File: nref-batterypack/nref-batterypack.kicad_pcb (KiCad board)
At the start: 2 copper layers, 75 x 17 mm, 53 parts, among them J1 C3-, J2 DBG, J3 PACK_CONN, J4 C4+, J5 C2+, J6 C1-, J7 C1-, J8 BACK_CONN, SW1 Reset, U1 BQ76905, U2 TPS259482, U3 MSPM0L130xRGE

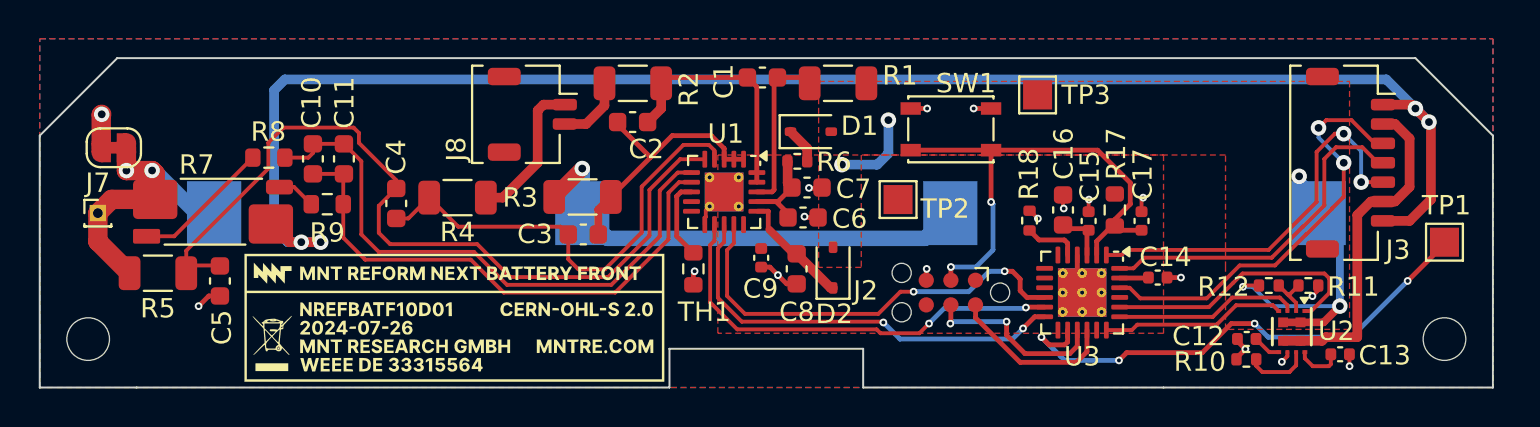
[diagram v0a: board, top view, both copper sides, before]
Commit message: v2 of the bms now based on the final outline
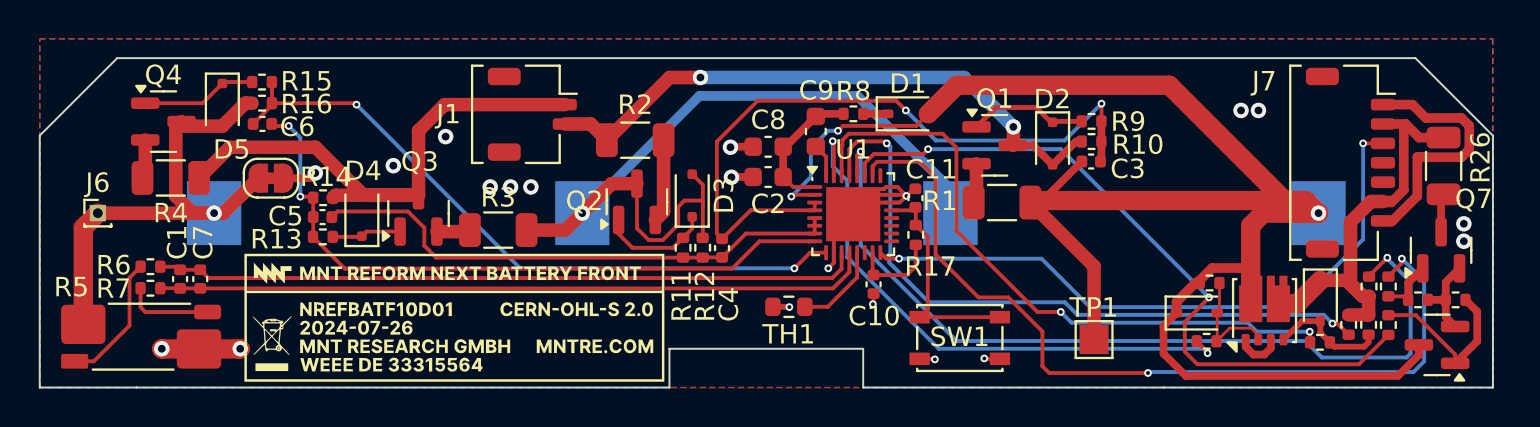
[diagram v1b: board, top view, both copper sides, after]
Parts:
- removed C12: 2.2nF, Capacitor_SMD:C_0402_1005Metric
- removed C13: DNP, Capacitor_SMD:C_0402_1005Metric
- removed C14: 0.47uF, Capacitor_SMD:C_0402_1005Metric
- removed C15, C17: 100nF, Capacitor_SMD:C_0402_1005Metric
- removed C16: 10uF, Capacitor_SMD:C_0603_1608Metric
- removed the J2 at (147.0, 103.1)
- removed REF** (x2): MountingHole_2.2mm_M2, MountingHole:MountingHole_2.2mm_M2
- removed TP2: 3V3, TestPoint:TestPoint_Pad_1.5x1.5mm
- removed TP3: Pack Voltage, TestPoint:TestPoint_Pad_1.5x1.5mm
- removed U2: TPS259482, Automated:PowerWCSP12_YWP_TEX
- removed U3: MSPM0L130xRGE, Package_DFN_QFN:VQFN-24-1EP_4x4mm_P0.5mm_EP2.5x2.5mm_ThermalVias
- added D3: 30V, Diode_SMD:D_SOD-323F, F.Cu at (133.7, 98.1)
- added D4: 30V, Diode_SMD:D_SOD-323F, F.Cu at (116.6, 99.1)
- added D5: 30V, Diode_SMD:D_SOD-323F, F.Cu at (109.4, 93.4)
- added D6: 16V, Diode_SMD:D_SOD-323, F.Cu at (159.7, 104.2)
- added D7: 16V, Diode_SMD:D_SOD-323, F.Cu at (166.1, 103.5)
- added Q1: BC817, Package_TO_SOT_SMD:SOT-23, F.Cu at (149.3, 95.5)
- added Q2: BC817, Package_TO_SOT_SMD:SOT-23, F.Cu at (130.8, 98.4)
- added Q3: BC817, Package_TO_SOT_SMD:SOT-23, F.Cu at (119.5, 99.0)
- added Q4: BC817, Package_TO_SOT_SMD:SOT-23, F.Cu at (106.4, 94.3)
- added Q5: AO3401A, Package_TO_SOT_SMD:SOT-23, F.Cu at (172.1, 105.8)
- added Q6: DMT2005UDV, Automated:Diodes_PowerDI3333-8_UXC_3.3x3.3mm_P0.65mm, F.Cu at (163.2, 104.0)
- added Q7: AO3401A, Package_TO_SOT_SMD:SOT-23, F.Cu at (172.3, 100.9)
- added R13: 240R, Resistor_SMD:R_0402_1005Metric, F.Cu at (114.6, 100.2)
- added R14: 100R, Resistor_SMD:R_0402_1005Metric, F.Cu at (114.6, 98.2)
- added R15: 240R, Resistor_SMD:R_0402_1005Metric, F.Cu at (111.5, 92.2)
- added R16: 100R, Resistor_SMD:R_0402_1005Metric, F.Cu at (111.5, 93.3)
- added R19: 5.1k, Resistor_SMD:R_0402_1005Metric, F.Cu at (169.6, 104.8)
- added R20: 5.1k, Resistor_SMD:R_0402_1005Metric, F.Cu at (160.2, 105.6)
- added R21: 10M, Resistor_SMD:R_0402_1005Metric, F.Cu at (173.1, 103.5)
- added R22: 10M, Resistor_SMD:R_0402_1005Metric, F.Cu at (171.1, 103.5)
- added R23: 5.1k, Resistor_SMD:R_0402_1005Metric, F.Cu at (166.1, 105.7)
- added R24: 5.1k, Resistor_SMD:R_0402_1005Metric, F.Cu at (169.6, 102.8)
- added R25: 10M, Resistor_SMD:R_0402_1005Metric, F.Cu at (168.6, 104.8)
- added R26: 1k, Resistor_SMD:R_1206_3216Metric, F.Cu at (172.5, 96.6)
- added R27: 10k, Resistor_SMD:R_0402_1005Metric, F.Cu at (168.6, 102.8)
- added R28: 10k, Resistor_SMD:R_0402_1005Metric, F.Cu at (167.6, 104.8)
- C1: value 220nF -> 100nF; footprint Capacitor_SMD:C_0603_1608Metric -> Capacitor_SMD:C_0402_1005Metric
- C10: value 100pF -> 2.2uF; footprint Capacitor_SMD:C_0603_1608Metric -> Capacitor_SMD:C_0402_1005Metric
- C11, C3, C4, C5: footprint Capacitor_SMD:C_0603_1608Metric -> Capacitor_SMD:C_0402_1005Metric
- C2: value 220nF -> 100pF/25V
- C6: value 100pF/25V -> 220nF; footprint Capacitor_SMD:C_0603_1608Metric -> Capacitor_SMD:C_0402_1005Metric
- C7: value 1uF/25V -> 100pF; footprint Capacitor_SMD:C_0603_1608Metric -> Capacitor_SMD:C_0402_1005Metric
- C9: value 1uF -> 470nF/25V; footprint Capacitor_SMD:C_0402_1005Metric -> Capacitor_SMD:C_0603_1608Metric
- D2: value 40V -> 30V; footprint Diode_SMD:D_SOD-323 -> Diode_SMD:D_SOD-323F
- R1, R2, R3, R4: value 10R -> 49.9R
- R10: value 866R -> 100R
- R11: value 14.7k -> 240R
- R12: value 470k -> 100R
- R17, R8: footprint Resistor_SMD:R_0603_1608Metric -> Resistor_SMD:R_0402_1005Metric
- R18: value 100k/0.1%/25ppm -> 10M
- R5: value 10R -> 1u; footprint Resistor_SMD:R_1206_3216Metric -> Resistor_SMD:R_Shunt_Vishay_WSK2512_6332Metric_T1.19mm
- R7: value 1u -> 100R; footprint Resistor_SMD:R_Shunt_Vishay_WSK2512_6332Metric_T1.19mm -> Resistor_SMD:R_0402_1005Metric
- R9: value 100R -> 240R; footprint Resistor_SMD:R_0603_1608Metric -> Resistor_SMD:R_0402_1005Metric
- TP1: value BSL Invoke -> Pack Voltage
- U1: value BQ76905 -> BQ76922; footprint Package_DFN_QFN:QFN-20-1EP_3.5x3.5mm_P0.5mm_EP2x2mm_ThermalVias -> Package_DFN_QFN:Texas_RSN_WQFN-32-1EP_4x4mm_P0.4mm_EP2.8x2.8mm
- moved R9 39.7 mm to (154.3, 94.3), turned to 180 degrees
- moved R6 33.8 mm to (105.7, 101.8)
- moved R11 32.3 mm to (133.2, 100.8), turned to 90 degrees
- moved C1 31.8 mm to (107.2, 102.4), turned to -90 degrees
- moved C7 31.7 mm to (108.3, 102.4), turned to -90 degrees
- moved R8 30.3 mm to (142.0, 93.9)
- moved C10 29.7 mm to (143.0, 102.7), turned to 90 degrees
- moved C11 29.6 mm to (145.2, 98.2)
- moved R12 29.3 mm to (134.2, 100.8), turned to 90 degrees
- moved C6 28.3 mm to (111.5, 94.4), turned to 180 degrees
- moved C3 26.5 mm to (154.3, 96.3), turned to 0 degrees
- moved TP1 18.8 mm to (154.4, 105.5)
- moved C4 17.0 mm to (135.2, 100.8), turned to -90 degrees
- moved R4 14.8 mm to (106.8, 97.2), turned to 180 degrees
- moved R10 13.8 mm to (154.3, 95.3), turned to 180 degrees
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- renumbered J8 to J1, J4 to J2, J1 to J3, J5 to J4, J6 to J5, J7 to J6, J3 to J7
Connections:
- net /V_{OUT} renamed /PACK+
- C1 pad 1: Net-(U1-VC5) -> /SRP
- C1 pad 2: Net-(U1-VC4A) -> /SRN
- C10 pad 1: Net-(U1-SRP) -> GND
- C10 pad 2: Net-(U1-SRN) -> +1V8
- C11 pad 1: Net-(U1-SRP) -> GND
- C11 pad 2: Net-(U1-SRN) -> /~{RST}
- C2 pad 1: Net-(U1-VC4A) -> Net-(U1-BAT)
- C2 pad 2: Net-(U1-VC2) -> GND
- C3 pad 1: Net-(U1-VC2) -> /BAT+
- C3 pad 2: Net-(U1-VC1) -> /VC4
- C4 pad 1: Net-(U1-VC1) -> /VC4
- C4 pad 2: Net-(U1-VC0) -> /VC2
- C5 pad 1: Net-(U1-VC0) -> /VC2
- C5 pad 2: GND -> /VC1
- C6 pad 1: Net-(U1-BAT) -> /VC1
- C6 pad 2: GND -> /VC0
- C7 pad 1: Net-(U1-BAT) -> /SRP
- C7 pad 2: GND -> /SRN
- C8 pad 1: /REGSRC -> Net-(U1-BAT)
- C9 pad 1: +3V3 -> Net-(U1-CP1)
- C9 pad 2: GND -> Net-(U1-BAT)
- D1 pad 2: IN -> /BAT+
- D2 pad 1: /REGSRC -> Net-(D2-K)
- D2 pad 2: IN -> /C3+
- J2 pad 1: IN -> /BAT+
- J3 pad 1: /C2+ -> Net-(D3-A)
- J4 pad 1: /C2+ -> Net-(D3-A)
- J7 pad 3: /IRQ -> /ALERT
- R1 pad 1: Net-(U1-VC5) -> /BAT+
- R1 pad 2: IN -> Net-(Q1-C)
- R10 pad 1: GND -> /VC4
- R10 pad 2: Net-(U2-ILM) -> /C3+
- R11 pad 1: GND -> /VC2
- R11 pad 2: Net-(U2-OVLO) -> Net-(D3-K)
- R12 pad 1: Net-(U2-OVLO) -> /VC2
- R12 pad 2: IN -> Net-(D3-A)
- R17 pad 2: +3V3 -> +1V8
- R18 pad 1: GND -> Net-(D6-A)
- R18 pad 2: Net-(U3-PA2) -> /BAT+
- R2 pad 1: Net-(U1-VC4A) -> /C3+
- R2 pad 2: /C3+ -> Net-(Q2-C)
- R3 pad 1: Net-(U1-VC2) -> Net-(D3-A)
- R3 pad 2: /C2+ -> Net-(Q3-C)
- R4 pad 1: Net-(U1-VC1) -> /C1+
- R4 pad 2: /C1+ -> Net-(Q4-C)
- R5 pad 1: Net-(U1-VC0) -> /BAT-
- R5 pad 2: /BAT- -> Net-(R5-Pad2)
- R6 pad 1: Net-(U1-BAT) -> Net-(R5-Pad2)
- R6 pad 2: Net-(D1-K) -> /SRP
- R7 pad 1: /BAT- -> Net-(R5-Pad3)
- R7 pad 2: Net-(R7-Pad2) -> /SRN
- R8 pad 1: Net-(R7-Pad2) -> Net-(U1-BAT)
- R8 pad 2: Net-(U1-SRP) -> Net-(D1-K)
- R9 pad 1: Net-(R7-Pad3) -> /VC4
- R9 pad 2: Net-(U1-SRN) -> Net-(D2-K)
- TH1 pad 1: Net-(U1-TS) -> Net-(U1-TS1)
- TP1 pad 1: /BSL_INVOKE -> /BAT+
- U1 pad 1: Net-(U1-VC2) -> Net-(U1-BAT)
- U1 pad 10: unconnected-(U1-CHG-Pad10) -> GND
- U1 pad 11: GND -> /SRP
- U1 pad 12: /SCL_{DEV} -> /SRN
- U1 pad 13: /SDA_{DEV} -> Net-(U1-TS1)
- U1 pad 14: /ALERT -> unconnected-(U1-TS2-Pad14)
- U1 pad 15: +3V3 -> +1V8
- U1 pad 16: /REGSRC -> /ALERT
- U1 pad 17: Net-(U1-BAT) -> /SCL_{DEV}
- U1 pad 18: Net-(U1-VC5) -> /SDA_{DEV}
- U1 pad 19: Net-(U1-VC4A) -> unconnected-(U1-CFETOFF-Pad19)
- U1 pad 2: Net-(U1-VC2) -> /BAT+
- U1 pad 20: Net-(U1-VC4A) -> unconnected-(U1-DFETOFF-Pad20)
- U1 pad 21: GND -> /~{RST}
- U1 pad 3: Net-(U1-VC2) -> /VC4
- U1 pad 4: Net-(U1-VC1) -> /VC4
- U1 pad 5: Net-(U1-VC0) -> /VC2
- U1 pad 6: Net-(U1-SRP) -> /VC2
- U1 pad 7: Net-(U1-SRN) -> /VC2
- U1 pad 8: Net-(U1-TS) -> /VC1
- U1 pad 9: unconnected-(U1-DSG-Pad9) -> /VC0
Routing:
- net /BAT+: track 0.00 -> 93.2 mm, vias 0 -> 3
- net /PACK-: track 83.3 -> 17.4 mm, vias 4 -> 11
- net /PDSG: track 0.00 -> 44.2 mm, vias 0 -> 2
- net /LD: track 0.00 -> 43.8 mm, vias 0 -> 2
- net Net-(U1-VC0): track 43.5 -> 0.00 mm
- net Net-(D3-A): track 0.00 -> 42.3 mm, vias 0 -> 1
- net /SRN: track 0.00 -> 36.9 mm
- net /PCHG: track 0.00 -> 36.6 mm, vias 0 -> 2
- net /SRP: track 0.00 -> 36.4 mm
- net /VC4: track 0.00 -> 36.3 mm, vias 0 -> 2
- net /VC0: track 0.00 -> 35.0 mm, vias 0 -> 2
- net /PACK: track 0.00 -> 35.0 mm, vias 0 -> 2
- net /VC1: track 0.00 -> 34.7 mm, vias 0 -> 2
- net /DSG: track 0.00 -> 33.4 mm, vias 0 -> 2
- net Net-(U1-SRP): track 30.6 -> 0.00 mm
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- added copper zone on B.Cu, net /PACK-
- added copper zone on In1.Cu, net GND
- added copper zone on In2.Cu, net GND
- removed copper zone on F.Cu, net +3V3
- removed copper zone on B.Cu, net GND
- removed copper zone on F.Cu, net IN
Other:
- copper layers 2 -> 4

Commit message: batterypack: pick parts
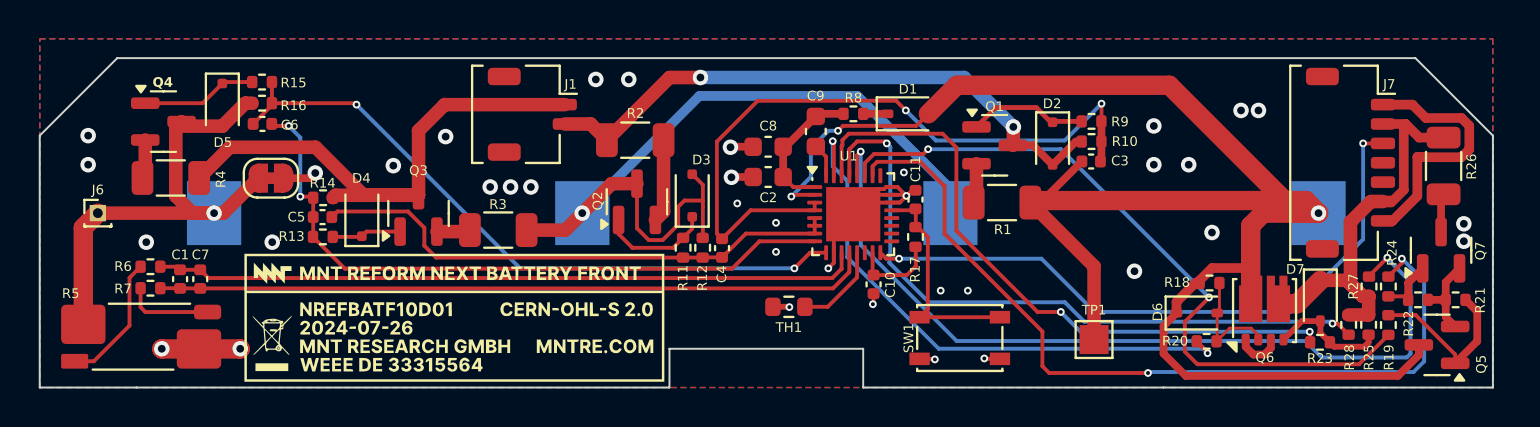
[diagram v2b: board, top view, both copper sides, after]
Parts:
- moved R17 0.11 mm to (145.2, 100.2)
- moved C11 0.08 mm to (145.2, 98.3)
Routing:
- net /PDSG: track 44.2 -> 43.3 mm
- net GND: vias 9 -> 15
- net /PACK-: vias 11 -> 22

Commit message: fix load switch nmos and gate prot diode polarity
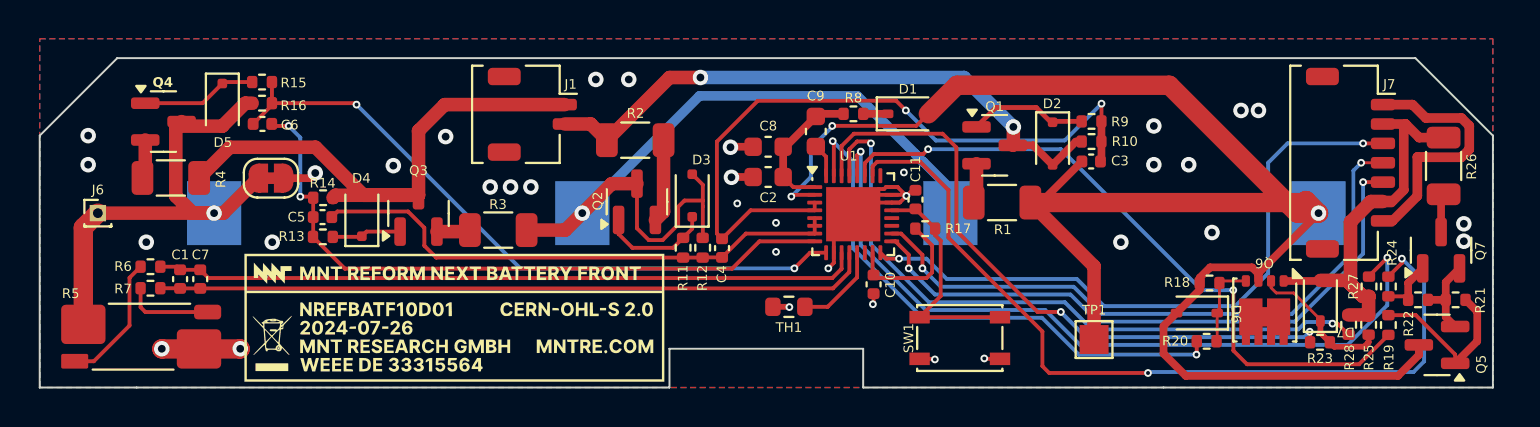
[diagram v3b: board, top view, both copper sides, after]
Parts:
- moved R17 0.66 mm to (145.7, 99.8), turned to 180 degrees
- turned Q6 to -90 degrees
- turned D6 to 180 degrees
- turned D7 to 90 degrees
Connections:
- D6 pad 1: /BAT+ -> Net-(D6-K)
- D6 pad 2: Net-(D6-A) -> /BAT+
- D7 pad 1: /PACK+ -> Net-(D7-K)
- D7 pad 2: Net-(D7-A) -> /PACK+
- J7 pad 4: /SDA_{HOST} -> /SDA
- J7 pad 5: /SCL_{HOST} -> /SCL
- Q6 pad 1: Net-(Q6A-S) -> /PACK+
- Q6 pad 2: Net-(D6-A) -> Net-(D7-K)
- Q6 pad 3: Net-(Q6A-S) -> /BAT+
- Q6 pad 4: Net-(D7-A) -> Net-(D6-K)
- Q6 pad 5: /PACK+ -> Net-(Q6A-D)
- Q6 pad 6: /BAT+ -> Net-(Q6A-D)
- R18 pad 1: Net-(D6-A) -> Net-(D6-K)
- R20 pad 2: Net-(D6-A) -> Net-(D6-K)
- R23 pad 2: Net-(D7-A) -> Net-(D7-K)
- R25 pad 1: Net-(D7-A) -> Net-(D7-K)
- U1 pad 17: /SCL_{DEV} -> /SCL
- U1 pad 18: /SDA_{DEV} -> /SDA
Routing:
- net /SDA: track 0.00 -> 33.2 mm, vias 0 -> 2
- net /SCL: track 0.00 -> 32.6 mm, vias 0 -> 2
- net Net-(D7-K): track 0.00 -> 7.53 mm
- net Net-(D7-A): track 6.18 -> 0.00 mm
- net Net-(D6-A): track 5.89 -> 0.00 mm
- net Net-(D6-K): track 0.00 -> 4.48 mm
- net /LD: track 43.8 -> 40.1 mm
- net /BAT+: track 93.2 -> 89.6 mm
- net Net-(Q6A-S): track 2.40 -> 0.00 mm
- net +1V8: track 4.64 -> 7.00 mm
- net /PCHG: track 36.6 -> 35.0 mm
- net Net-(Q6A-D): track 0.00 -> 1.43 mm
- net /CHG: track 29.6 -> 28.5 mm
- net /PACK+: track 21.9 -> 21.2 mm
- net GND: vias 15 -> 13

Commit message: added reverse polarity indicator LEDs
+ silk on the back to indicate cell polarity
+ updated resistor values for balancing
* better b2b chg, dsg fets
+ more testpoints
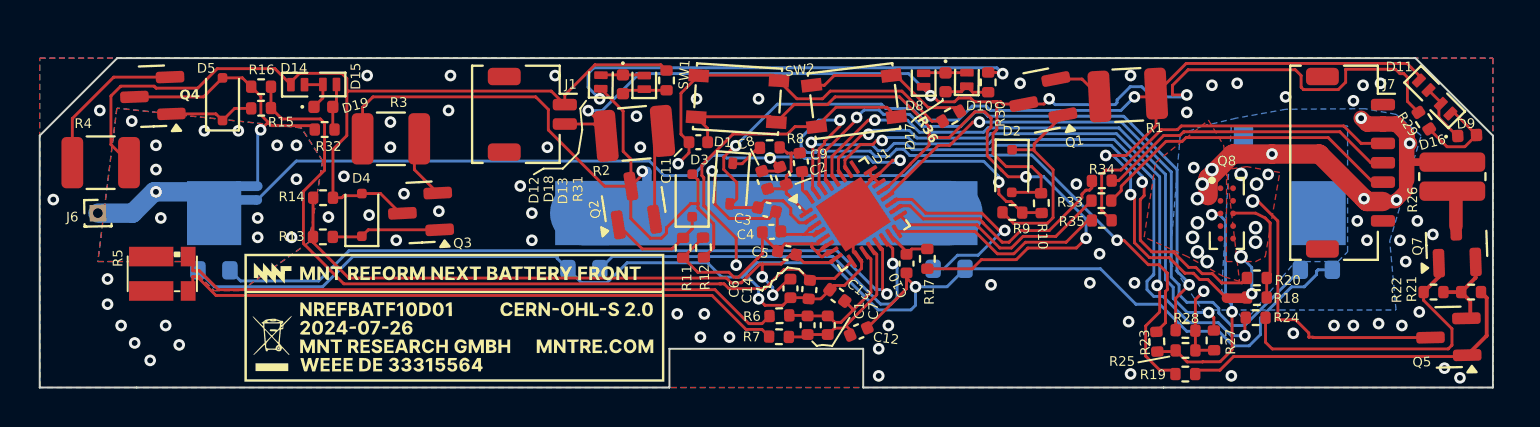
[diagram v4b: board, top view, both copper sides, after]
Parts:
- removed D6, D7: 16V, Diode_SMD:D_SOD-323
- removed Q6: DMT2005UDV, Automated:Diodes_PowerDI3333-8_UXC_3.3x3.3mm_P0.65mm
- added C12: 100nF, Capacitor_SMD:C_0402_1005Metric, F.Cu at (142.3, 105.1)
- added C13: 100nF, Capacitor_SMD:C_0402_1005Metric, F.Cu at (141.2, 103.2)
- added C14: 100nF, Capacitor_SMD:C_0402_1005Metric, F.Cu at (139.7, 102.9)
- added D10: BAS70LP, Diode_SMD:D_SOD-882, F.Cu at (147.8, 92.1)
- added D11: BAS70LP, Diode_SMD:D_SOD-882, F.Cu at (171.4, 92.4)
- added D12: BAS70LP, Diode_SMD:D_SOD-882, F.Cu at (129.0, 92.2)
- added D13: BAS70LP, Diode_SMD:D_SOD-882, F.Cu at (131.2, 92.2)
- added D14: BAS70LP, Diode_SMD:D_SOD-882, F.Cu at (113.3, 92.4)
- added D15: BAS70LP, Diode_SMD:D_SOD-882, F.Cu at (115.0, 92.4)
- added D16: BAS70LP, Diode_SMD:D_SOD-882, F.Cu at (172.6, 93.6)
- added D17: Red, LED_SMD:LED_0402_1005Metric, F.Cu at (146.8, 92.2)
- added D18: Red, LED_SMD:LED_0402_1005Metric, F.Cu at (130.1, 92.3)
- added D19: Red, LED_SMD:LED_0402_1005Metric, F.Cu at (114.6, 93.5)
- added D8: BAS70LP, Diode_SMD:D_SOD-882, F.Cu at (145.6, 92.1)
- added D9: Red, LED_SMD:LED_0402_1005Metric, F.Cu at (173.7, 95.0)
- added NT3: P- to GND, NetTie:NetTie-2_SMD_Pad0.5mm, B.Cu at (131.3, 97.3)
- added NT4.0: P- to GND, NetTie:NetTie-2_SMD_Pad0.5mm, F.Cu at (161.8, 103.4)
- added NT5: P- to GND, NetTie:NetTie-2_SMD_Pad0.5mm, B.Cu at (110.8, 97.6)
- added Q8: Q_Dual_NMOS_Picostar_CSD87501L, Automated:TI_PICOSTAR_LGA-10_3.37x1.47mm_P0.65mm, F.Cu at (161.3, 99.0)
- added R29: 100, Resistor_SMD:R_0402_1005Metric, F.Cu at (171.4, 94.2)
- added R30: 100, Resistor_SMD:R_0402_1005Metric, F.Cu at (148.9, 92.2)
- added R31: 100, Resistor_SMD:R_0402_1005Metric, F.Cu at (132.3, 92.2)
- added R32: 100, Resistor_SMD:R_0402_1005Metric, F.Cu at (114.7, 94.7)
- added R33: 100, Resistor_SMD:R_0402_1005Metric, F.Cu at (154.8, 98.4)
- added R34: 100, Resistor_SMD:R_0402_1005Metric, F.Cu at (154.8, 97.3)
- added R35: 100, Resistor_SMD:R_0402_1005Metric, F.Cu at (154.8, 99.4)
- added R36: 10k, Resistor_SMD:R_0402_1005Metric, F.Cu at (147.0, 94.0)
- added SW2: Wake, Button_Switch_SMD:SW_SPST_PTS810, F.Cu at (142.0, 93.2)
- added TH2: Thermistor, Resistor_SMD:R_0603_1608Metric, B.Cu at (128.1, 101.9)
- added TH3: Thermistor, Resistor_SMD:R_0603_1608Metric, B.Cu at (146.9, 101.9)
- added TH4: Thermistor, Resistor_SMD:R_0603_1608Metric, B.Cu at (165.9, 101.9)
- C2: value 100pF/25V -> 100pF; footprint Capacitor_SMD:C_0603_1608Metric -> Capacitor_SMD:C_0402_1005Metric
- C3, C4, C5, C6: value 220nF -> 100nF
- C8: value 1uF/25V -> 2.2uF/25V; footprint Capacitor_SMD:C_0603_1608Metric -> Capacitor_SMD:C_0402_1005Metric
- C9: footprint Capacitor_SMD:C_0603_1608Metric -> Capacitor_SMD:C_0402_1005Metric
- D2, D3, D4, D5: value 30V -> BAS70LP
- J2, J3, J4, J5: footprint footprints:S713145R -> Automated:S713145R
- NT1: value P- to GND -> P- to VSS; footprint Jumper:SolderJumper-2_P1.3mm_Bridged_RoundedPad1.0x1.5mm -> NetTie:NetTie-2_SMD_Pad0.5mm; moved to B.Cu
- R1, R2, R3, R4: value 49.9R -> 39; footprint Resistor_SMD:R_1206_3216Metric -> Resistor_SMD:R_1210_3225Metric
- R10, R12, R14, R16, R17, R6, R7, R8: value 100R -> 100
- R11, R13, R15, R9: value 240R -> 240
- R19, R20, R23, R24: value 5.1k -> 1k
- R26: value 1k -> 270; footprint Resistor_SMD:R_1206_3216Metric -> Resistor_SMD:R_0612_1632Metric
- R5: value 1u -> 15mΩ 1%; footprint Resistor_SMD:R_Shunt_Vishay_WSK2512_6332Metric_T1.19mm -> Automated:R_Shunt_Kelvin_Littlefuse_L4CA
- TH1: moved to B.Cu
- TP1: footprint TestPoint:TestPoint_Pad_1.5x1.5mm -> TestPoint:TestPoint_Pad_1.0x1.0mm; moved to B.Cu
- moved R6 32.6 mm to (138.2, 104.3), turned to 2 degrees
- moved R7 32.5 mm to (138.2, 105.4), turned to -1 degrees
- moved C1 32.5 mm to (139.6, 104.8)
- moved C7 32.5 mm to (140.7, 104.8)
- moved TH1 29.7 mm to (109.0, 101.9)
- moved C6 28.5 mm to (138.7, 102.9), turned to -90 degrees
- moved C5 24.0 mm to (138.6, 101.1), turned to -11.35 degrees
- moved C3 16.9 mm to (137.5, 98.8), turned to -12.8 degrees
- moved SW1 16.8 mm to (136.0, 93.1), turned to -3.6 degrees
- moved TP1 13.0 mm to (162.1, 95.0), turned to 89.3 degrees
- moved C11 11.6 mm to (134.0, 95.3), turned to 0 degrees
- moved R19 10.8 mm to (159.1, 107.3), turned to 0 degrees
- moved D1 9.80 mm to (135.7, 97.5), turned to -94.23 degrees
- moved R25 9.54 mm to (159.1, 106.1), turned to 0 degrees
- moved R1 8.54 mm to (156.2, 92.9), turned to -177 degrees
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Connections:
- net /PACK renamed /bqPACK
- net /SRN renamed /SR_N
- net /SRP renamed /SR_P
- net Net-(R5-Pad2) renamed /CSENSE_P
- net Net-(R5-Pad3) renamed /CSENSE_N
- net Net-(U1-BAT) renamed /bqBAT
- net Net-(U1-TS1) renamed /TS1
- C10 pad 1: GND -> VSS
- C2 pad 2: GND -> VSS
- C3 pad 1: /BAT+ -> /VC5
- C6 pad 2: /VC0 -> VSS
- C8 pad 2: GND -> VSS
- D1 pad 2: /BAT+ -> /VC5
- D3 pad 2: Net-(D3-A) -> Net-(D12-K)
- D5 pad 2: /BAT- -> Net-(D5-A)
- J2 pad 1: /BAT+ -> /BATplus
- J3 pad 1: Net-(D3-A) -> /Cell23
- J4 pad 1: Net-(D3-A) -> /Cell23
- J7 pad 1: /PACK- -> GND
- J7 pad 7: /PACK- -> GND
- NT1 pad 1: GND -> VSS
- Q2 pad 3: Net-(D3-A) -> Net-(D12-K)
- Q4 pad 3: /BAT- -> Net-(D5-A)
- Q5 pad 3: /BAT+ -> /BATplus
- R1 pad 1: /BAT+ -> /VC5
- R12 pad 2: Net-(D3-A) -> Net-(D12-K)
- R16 pad 2: /BAT- -> Net-(D5-A)
- R18 pad 2: /BAT+ -> /BATplus
- R3 pad 1: Net-(D3-A) -> Net-(D12-K)
- R5 pad 4: /PACK- -> GND
- TH1 pad 2: GND -> VSS
- TP1 pad 1: /BAT+ -> /BATplus
- U1 pad 10: GND -> VSS
- U1 pad 14: unconnected-(U1-TS2-Pad14) -> /TS2
- U1 pad 16: /ALERT -> Net-(U1-ALERT)
- U1 pad 17: /SCL -> Net-(U1-SCL)
- U1 pad 18: /SDA -> Net-(U1-SDA)
- U1 pad 19: unconnected-(U1-CFETOFF-Pad19) -> /TS3
- U1 pad 2: /BAT+ -> /VC5
- U1 pad 20: unconnected-(U1-DFETOFF-Pad20) -> /TS4
- U1 pad 22: GND -> VSS
- U1 pad 23: GND -> VSS
- U1 pad 24: GND -> VSS
- U1 pad 33: GND -> VSS
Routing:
- net VSS: track 0.00 -> 124.8 mm, vias 0 -> 4
- net /BAT+: track 89.6 -> 0.00 mm, vias 3 -> 0
- net /VC5: track 0.00 -> 63.4 mm, vias 0 -> 4
- net Net-(D12-K): track 0.00 -> 61.1 mm, vias 0 -> 3
- net Net-(D3-A): track 42.3 -> 0.00 mm, vias 1 -> 0
- net /TS2: track 0.00 -> 37.9 mm, vias 0 -> 2
- net /TS1: track 4.60 -> 38.5 mm, vias 0 -> 1
- net /C3+: track 31.3 -> 64.8 mm, vias 2 -> 4
- net /TS4: track 0.00 -> 32.0 mm, vias 0 -> 1
- net /~{RST}: track 12.0 -> 41.5 mm, vias 0 -> 2
- net /SR_P: track 36.4 -> 7.84 mm
- net /SR_N: track 36.9 -> 8.52 mm
- net /CSENSE_N: track 4.54 -> 31.9 mm
- net /CSENSE_P: track 6.87 -> 31.9 mm
- net /Cell23: track 0.00 -> 19.0 mm
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- added copper zone on B.Cu, net /BAT-
- added copper zone on F.Cu, net /BAT-
- added copper zone on B.Cu, net /BATplus
- added copper zone on F.Cu, net /BATplus
- added copper zone on B.Cu, net /PACK+
- added copper zone on F.Cu, net /PACK+
- added copper zone on B.Cu, net GND
- added copper zone on F.Cu, net GND
- removed copper zone on B.Cu, net /PACK-
- removed copper zone on F.Cu, net /PACK-
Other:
- board text added: "1"
- board text added: "2"
- board text added: "3"
- board text added: "4"
